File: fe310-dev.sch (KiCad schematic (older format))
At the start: 41 parts, among them J1 USB_B_Mini, J2 Conn_01x06, J3 Conn_01x12, J4 Conn_01x12, J5 Conn_01x08, SW1 SW_Push, U1 AMS1117-3.3, U2 AMS1117-1.8, U3 HT42B534, U4 FE310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

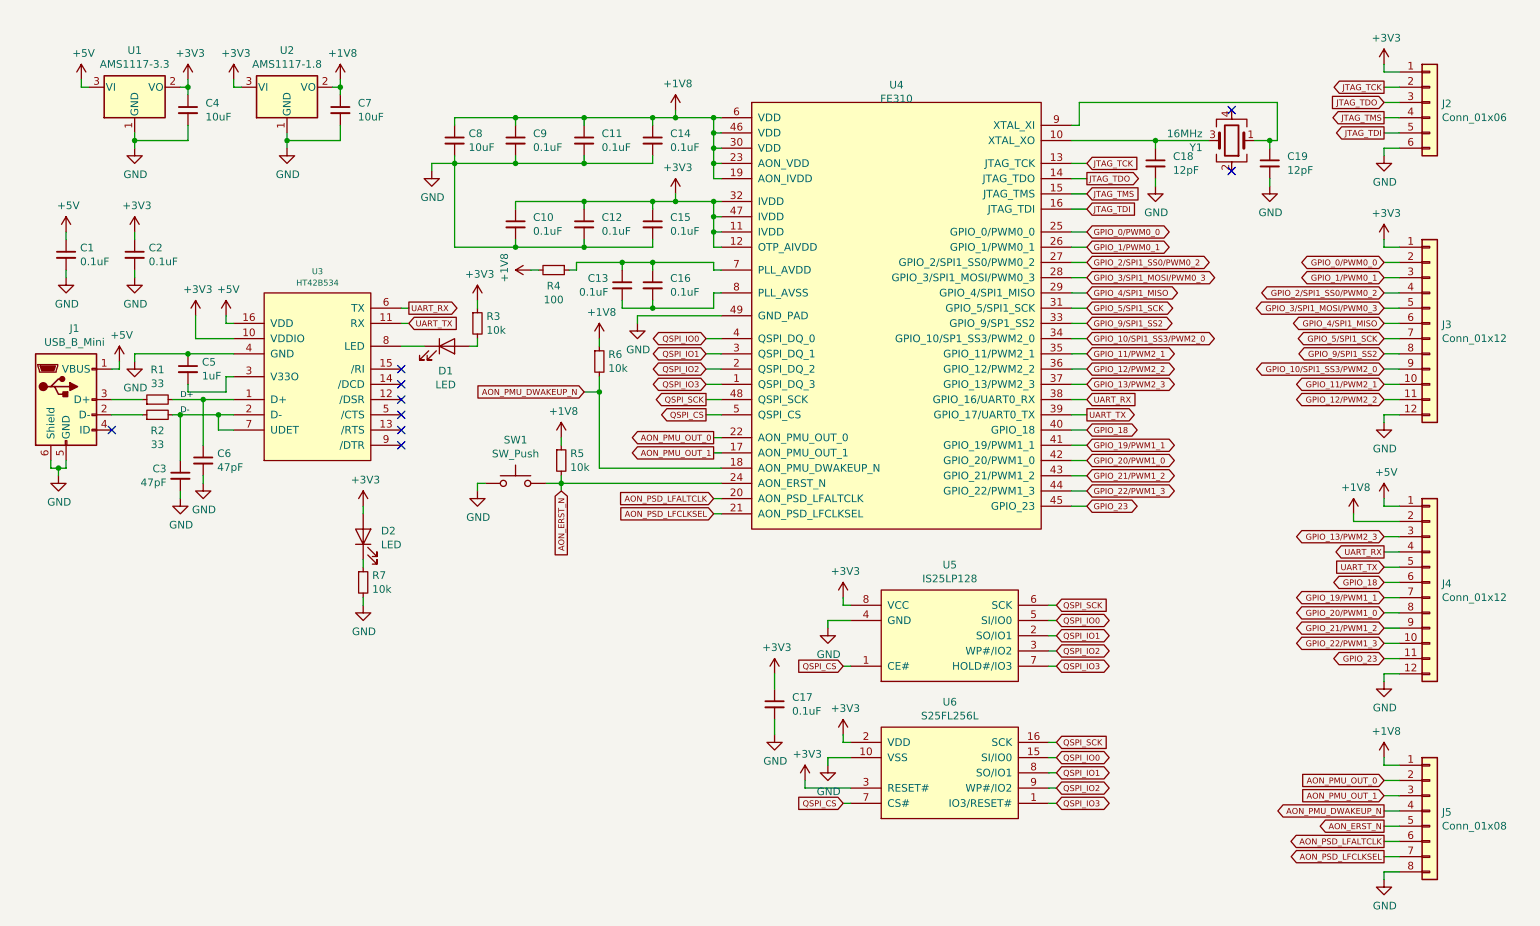
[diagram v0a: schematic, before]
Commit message: add jumper for selectable AON power domain voltage, which should work for #5
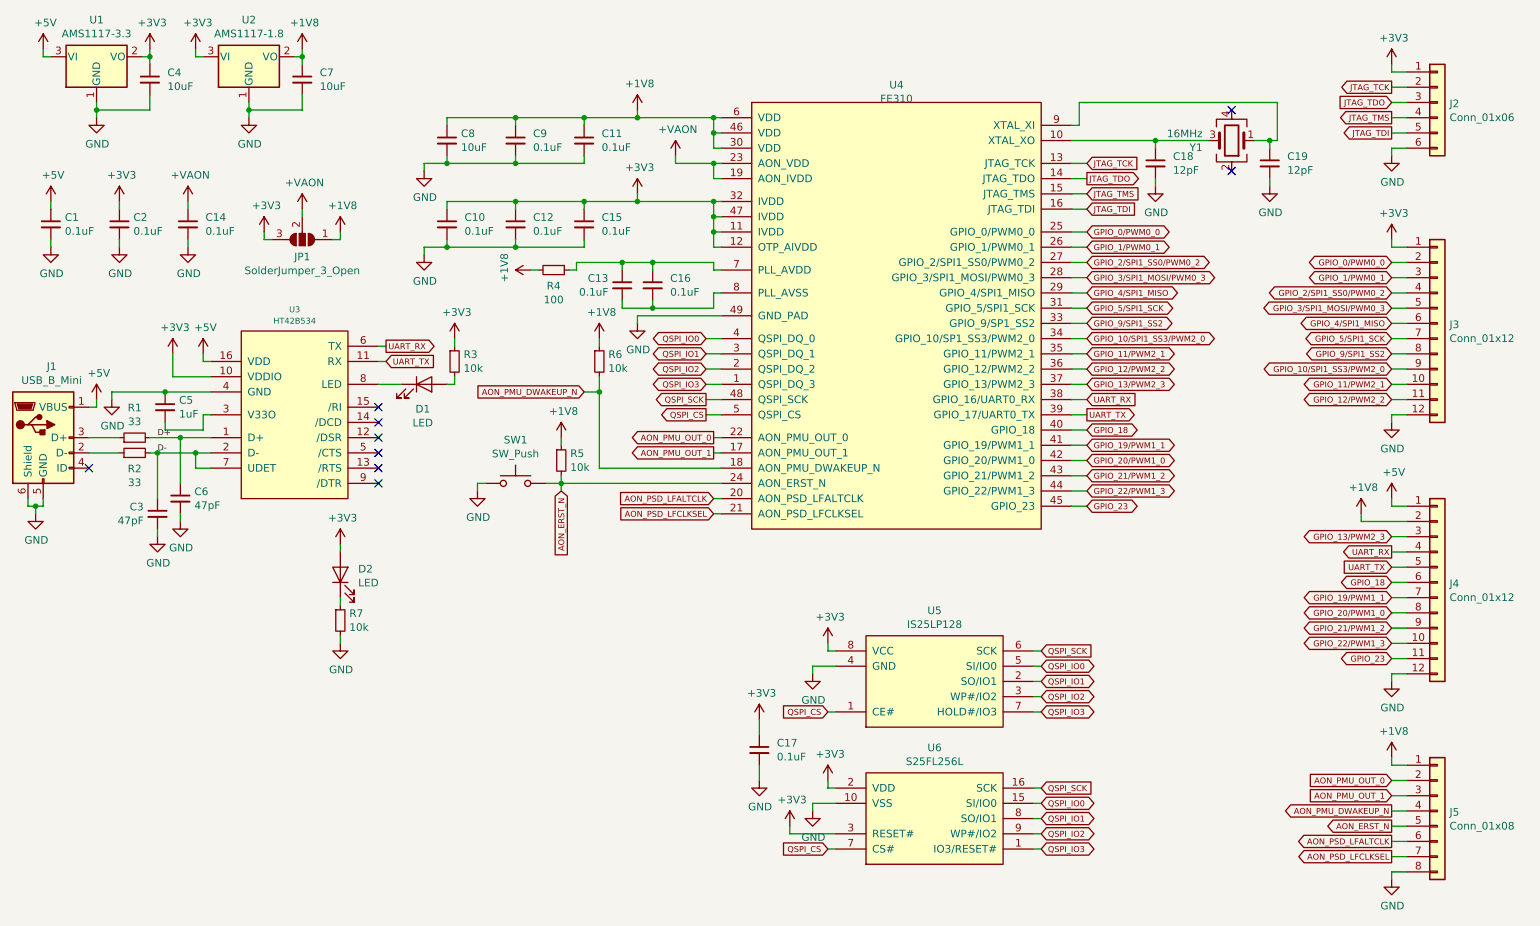
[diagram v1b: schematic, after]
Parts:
- added JP1: SolderJumper_3_Open, Jumper:SolderJumper-3_P1.3mm_Open_RoundedPad1.0x1.5mm, symbol Jumper:SolderJumper_3_Open
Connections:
- net +1V8: now also JP1.1 (A); no longer C14.1, U4.19 (AON_IVDD), U4.23 (AON_VDD)
- net +3V3: now also JP1.3 (B)
- new net +VAON: C14.1, JP1.2 (C), U4.19 (AON_IVDD), U4.23 (AON_VDD)
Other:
- moved on the sheet: C1, C10, C12, C14, C15, C17, C2, C3, C4, C5, C6, C7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

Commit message: pullup for AON_ERST_N should be connected to the AON i/o voltage
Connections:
- net +1V8: no longer R5.1
- net +VAON: now also R5.1
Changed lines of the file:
@@
 NoConn ~ 8550 1350
-$Comp
-L power:+1V8 #PWR0118
-U 1 1 5C03001D
-P 4150 3500
-F 0 "#PWR0118" H 4150 3350 50  0001 C CNN
-F 1 "+1V8" H 4165 3673 50  0000 C CNN
-F 2 "" H 4150 3500 50  0001 C CNN
-F 3 "" H 4150 3500 50  0001 C CNN
-	1    4150 3500
-	1    0    0    -1
-$EndComp
 $Comp
 L Device:R_Small R5
@@
 	1    0    0    -1
 $EndComp
-Wire Wire Line
-	4150 3550 4150 3500
 Wire Wire Line
 	5200 3800 4150 3800
@@
 Wire Wire Line
 	750  1000 750  950
+$Comp
+L fe310:+VAON #PWR?
+U 1 1 5DAFAE30
+P 4150 3500
+F 0 "#PWR?" H 4150 3350 50  0001 C CNN
+F 1 "+VAON" H 4165 3673 50  0000 C CNN
+F 2 "" H 4150 3500 50  0001 C CNN
+F 3 "" H 4150 3500 50  0001 C CNN
+	1    4150 3500
+	1    0    0    -1
+$EndComp
+Wire Wire Line
+	4150 3500 4150 3550
 $EndSCHEMATC

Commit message: same for AON wakeup pin...
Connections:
- net +1V8: no longer R6.1
- net +VAON: now also R6.1
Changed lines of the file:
@@
 Wire Wire Line
 	1650 4050 1650 4000
-$Comp
-L power:+1V8 #PWR0132
-U 1 1 5C24169E
-P 4400 2850
-F 0 "#PWR0132" H 4400 2700 50  0001 C CNN
-F 1 "+1V8" H 4415 3023 50  0000 C CNN
-F 2 "" H 4400 2850 50  0001 C CNN
-F 3 "" H 4400 2850 50  0001 C CNN
-	1    4400 2850
-	1    0    0    -1
-$EndComp
 Wire Wire Line
 	4400 3100 4400 3200
@@
 	750  1000 750  950
 $Comp
-L fe310:+VAON #PWR?
+L fe310:+VAON #PWR0118
 U 1 1 5DAFAE30
 P 4150 3500
-F 0 "#PWR?" H 4150 3350 50  0001 C CNN
+F 0 "#PWR0118" H 4150 3350 50  0001 C CNN
 F 1 "+VAON" H 4165 3673 50  0000 C CNN
 F 2 "" H 4150 3500 50  0001 C CNN
@@
 Wire Wire Line
 	4150 3500 4150 3550
+$Comp
+L fe310:+VAON #PWR?
+U 1 1 5DB27FF4
+P 4400 2850
+F 0 "#PWR?" H 4400 2700 50  0001 C CNN
+F 1 "+VAON" H 4415 3023 50  0000 C CNN
+F 2 "" H 4400 2850 50  0001 C CNN
+F 3 "" H 4400 2850 50  0001 C CNN
+	1    4400 2850
+	1    0    0    -1
+$EndComp
 $EndSCHEMATC
